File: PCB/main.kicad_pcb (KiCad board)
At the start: 2 copper layers, 100 x 100 mm, 73 parts, among them J1 Conn_01x10_Male, J2 Conn_01x33_Female, J3 Conn_01x33_Female, J4 Conn_01x33_Female, J5 Conn_01x33_Female, K1 G5NB, Q1 AO3401A, Q2 MMBT3904, Q3 FDS6690A, U1 LP2951-33DR, U2 AMS1117, U3 CH340G, U4 USB_Micro_B, U5 AT24C256C-SSHL-T, U6 LM358DR2G, U7 VL6180XV0NR_1, U8 MCP9700T-ETT, X1 12MHz Crystal

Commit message: Added QR Code.
Cleaned up PCB project structure. Just moved contents in main out to the root folder

Added to git ignore for autosave files
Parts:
- added G***: LOGO, Footprint_EEE3088F:QRCode, B.Cu at (127.0, 88.9)

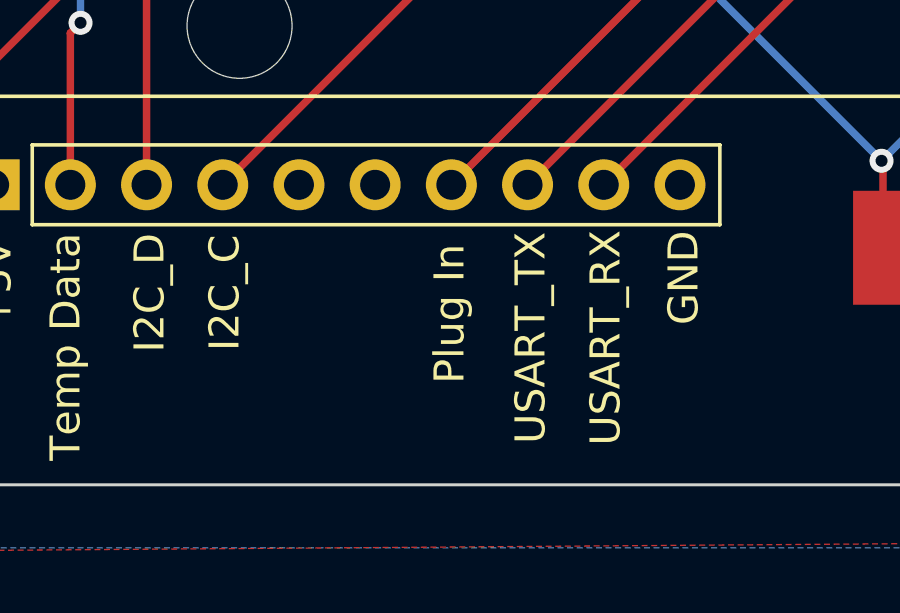
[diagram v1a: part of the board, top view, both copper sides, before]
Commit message: Labelled Test Points
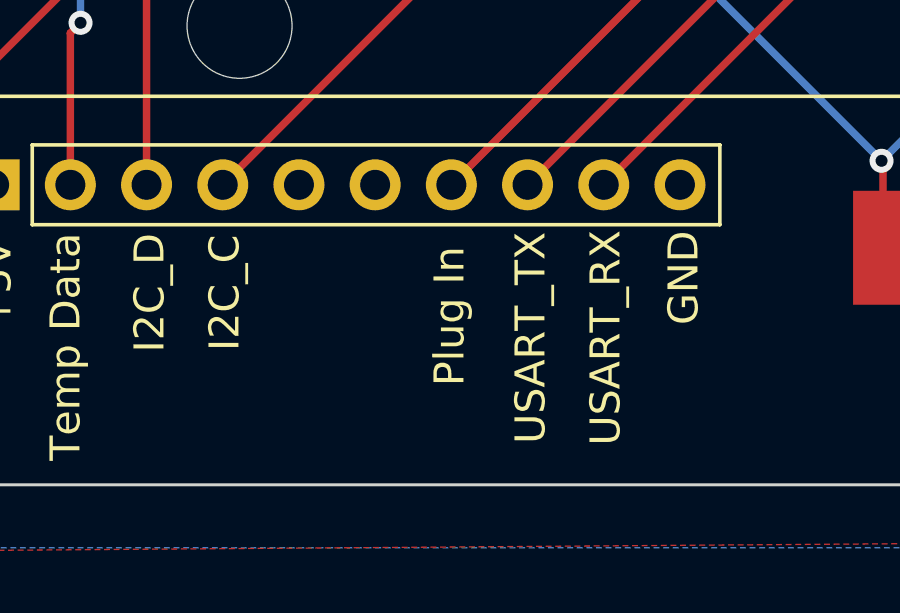
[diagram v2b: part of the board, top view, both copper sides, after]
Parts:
- TP1: value TestPoint -> BatPP
- TP2: value TestPoint -> 3.3V
- TP3: value TestPoint -> UsbOn
- TP4: value TestPoint -> CutP
- TP5: value TestPoint -> TempVcc
- TP6: value TestPoint -> TempOut
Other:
- board text added: "3.3V"
- board text added: "BatPP"
- board text added: "TempOut"
- board text added: "TempVcc"
- board text added: "UVCutPro"
- board text added: "UsbOn"
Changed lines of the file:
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@@
       (effects (font (size 1 1) (thickness 0.15)) (justify mirror))
     )
-    (fp_text value "TestPoint" (at 0 -1.55) (layer "B.Fab")
+    (fp_text value "3.3V" (at 0 -1.55) (layer "B.Fab")
       (effects (font (size 1 1) (thickness 0.15)) (justify mirror))
     )
@@
       (effects (font (size 1 1) (thickness 0.15)) (justify mirror))
     )
-    (fp_text value "TestPoint" (at 0 -1.55) (layer "B.Fab")
+    (fp_text value "TempOut" (at 0 -1.55) (layer "B.Fab")
       (effects (font (size 1 1) (thickness 0.15)) (justify mirror))
     )
@@
       (effects (font (size 1 1) (thickness 0.15)) (justify mirror))
     )
-    (fp_text value "TestPoint" (at 0 -1.55) (layer "B.Fab")
+    (fp_text value "BatPP" (at 0 -1.55) (layer "B.Fab")
       (effects (font (size 1 1) (thickness 0.15)) (justify mirror))
     )
@@
       (effects (font (size 1 1) (thickness 0.15)) (justify mirror))
     )
-    (fp_text value "TestPoint" (at 0 -1.55) (layer "B.Fab")
+    (fp_text value "TempVcc" (at 0 -1.55) (layer "B.Fab")
       (effects (font (size 1 1) (thickness 0.15)) (justify mirror))
     )
@@
       (effects (font (size 1 1) (thickness 0.15)) (justify mirror))
     )
-    (fp_text value "TestPoint" (at 0 -1.55) (layer "B.Fab")
+    (fp_text value "UsbOn" (at 0 -1.55) (layer "B.Fab")
       (effects (font (size 1 1) (thickness 0.15)) (justify mirror))
     )
@@
       (effects (font (size 1 1) (thickness 0.15)) (justify mirror))
     )
-    (fp_text value "TestPoint" (at 0 -1.55) (layer "B.Fab")
+    (fp_text value "CutP" (at 0 -1.55) (layer "B.Fab")
       (effects (font (size 1 1) (thickness 0.15)) (justify mirror))
     )
@@
   (gr_line (start 184.15 123.19) (end 95.25 123.19) (layer "F.Fab") (width 0.1))
   (gr_rect (start 173.99 91.44) (end 184.15 101.6) (layer "F.Fab") (width 0.1) (fill none))
+  (gr_text "3.3V\n" (at 157.48 98.5) (layer "B.SilkS")
+    (effects (font (size 0.7 0.7) (thickness 0.1)) (justify mirror))
+  )
+  (gr_text "UVCutPro" (at 151.13 147.1) (layer "B.SilkS")
+    (effects (font (size 0.7 0.7) (thickness 0.1)) (justify mirror))
+  )
+  (gr_text "TempOut" (at 153.67 112.3) (layer "B.SilkS")
+    (effects (font (size 0.7 0.7) (thickness 0.1)) (justify mirror))
+  )
+  (gr_text "TempVcc" (at 102.87 102.4) (layer "B.SilkS")
+    (effects (font (size 0.7 0.7) (thickness 0.1)) (justify mirror))
+  )
+  (gr_text "UsbOn" (at 168.91 90.17) (layer "B.SilkS")
+    (effects (font (size 0.7 0.7) (thickness 0.1)) (justify mirror))
+  )
+  (gr_text "BatPP" (at 169.545 150.495) (layer "B.SilkS")
+    (effects (font (size 0.7 0.7) (thickness 0.1)) (justify mirror))
+  )
   (gr_text "GND" (at 115.2 156.2 90) (layer "F.SilkS")
     (effects (font (size 1 1) (thickness 0.15)))
@@
     (effects (font (size 1 1) (thickness 0.15)))
   )
-  (gr_text "Plug In" (at 107.4 157.4 90) (layer "F.SilkS")
+  (gr_text "Plug In" (at 107.4 157.48 90) (layer "F.SilkS")
     (effects (font (size 1 1) (thickness 0.15)))
   )

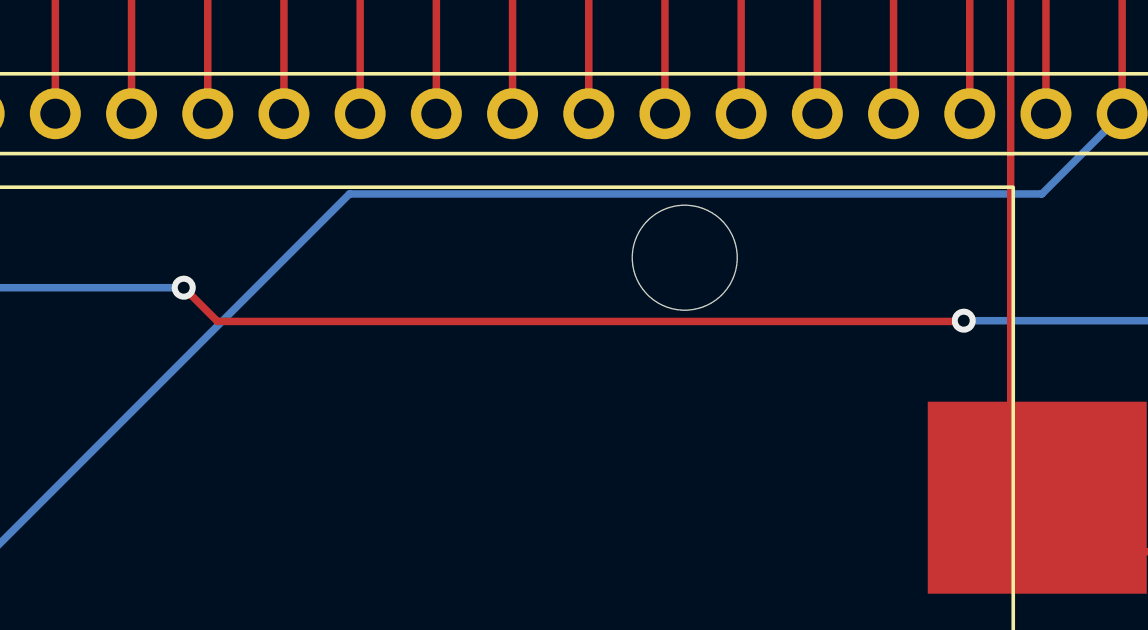
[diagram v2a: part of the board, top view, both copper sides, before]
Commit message: Fixed tp labels
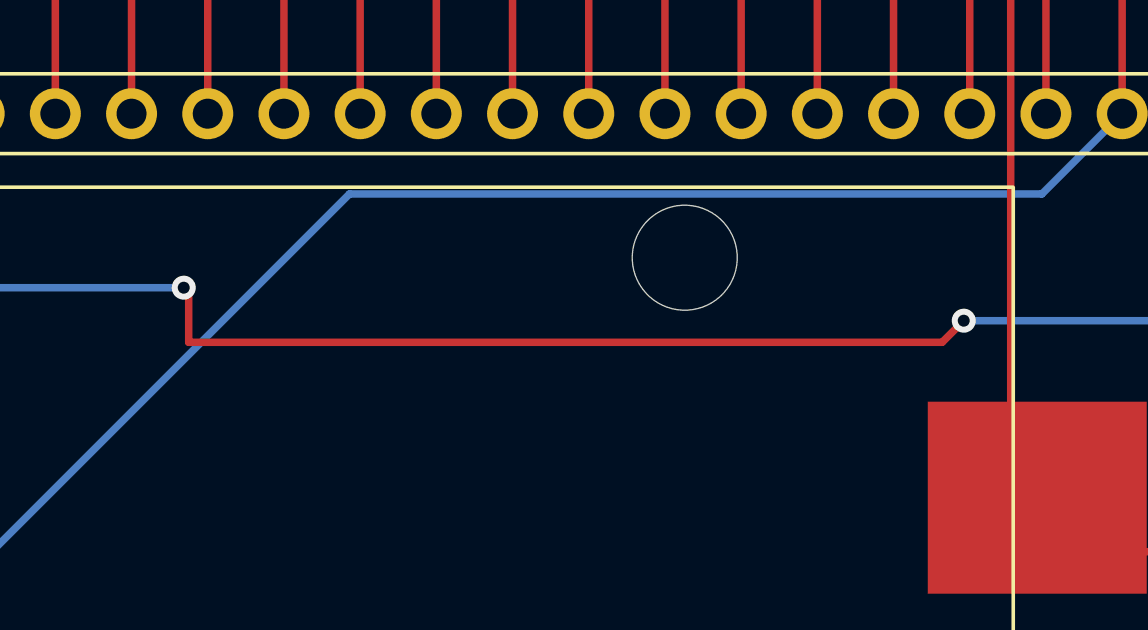
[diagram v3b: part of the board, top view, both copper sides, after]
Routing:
- net /microcontroller_interfacing/+5V: track 186.1 -> 187.7 mm
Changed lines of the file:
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@@
   (segment (start 179.3 101.3) (end 177.5 99.5) (width 0.25) (layer "F.Cu") (net 65))
   (segment (start 173.8 95.2) (end 171.8 93.2) (width 0.25) (layer "F.Cu") (net 65))
-  (segment (start 138.9 132.8) (end 140.024521 133.924521) (width 0.25) (layer "F.Cu") (net 65))
   (segment (start 177.5 96.3) (end 177.5 96.7) (width 0.25) (layer "F.Cu") (net 65))
   (segment (start 177.5 98.3) (end 177.5 96.7) (width 0.25) (layer "F.Cu") (net 65))
@@
   (segment (start 167.8 92.383928) (end 161.051072 85.635) (width 0.25) (layer "F.Cu") (net 65))
   (segment (start 161.051072 85.635) (end 160.675 85.635) (width 0.25) (layer "F.Cu") (net 65))
+  (segment (start 164.18 134.62) (end 164.9 133.9) (width 0.25) (layer "F.Cu") (net 65))
   (segment (start 157.573036 87.973036) (end 157.573036 93.453036) (width 0.25) (layer "F.Cu") (net 65))
-  (segment (start 140.024521 133.924521) (end 164.875479 133.924521) (width 0.25) (layer "F.Cu") (net 65))
   (segment (start 92.22 148.98) (end 108.4 132.8) (width 0.25) (layer "F.Cu") (net 65))
   (segment (start 178.3 97.7) (end 178.42 97.82) (width 0.25) (layer "F.Cu") (net 65))
+  (segment (start 139.065 134.62) (end 164.18 134.62) (width 0.25) (layer "F.Cu") (net 65))
   (segment (start 173.8 95.2) (end 176.4 95.2) (width 0.25) (layer "F.Cu") (net 65))
   (segment (start 157.573036 87.973036) (end 156.101072 89.445) (width 0.25) (layer "F.Cu") (net 65))
+  (segment (start 139.065 132.965) (end 139.065 134.62) (width 0.25) (layer "F.Cu") (net 65))
+  (segment (start 138.9 132.8) (end 139.065 132.965) (width 0.25) (layer "F.Cu") (net 65))
   (segment (start 177.5 98.5) (end 177.5 98.3) (width 0.25) (layer "F.Cu") (net 65))
   (segment (start 180.3 101.3) (end 179.3 101.3) (width 0.25) (layer "F.Cu") (net 65))
   (segment (start 177.5 96.9) (end 178.3 97.7) (width 0.25) (layer "F.Cu") (net 65))
   (segment (start 177.5 96.7) (end 177.5 96.9) (width 0.25) (layer "F.Cu") (net 65))
-  (segment (start 164.875479 133.924521) (end 164.9 133.9) (width 0.25) (layer "F.Cu") (net 65))
   (segment (start 156.101072 89.445) (end 155.725 89.445) (width 0.25) (layer "F.Cu") (net 65))
   (segment (start 174.7 101.3) (end 177.5 98.5) (width 0.25) (layer "F.Cu") (net 65))

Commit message: Fixed QR Code
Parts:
- moved G*** 1.42 mm to (126.4, 87.6)
